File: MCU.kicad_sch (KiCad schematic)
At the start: 19 parts, among them J1 Conn_01x04, J5 Conn_01x03_Pin, J6 Conn_01x03_Pin, J7 Conn_01x03_Pin, J8 Conn_01x04, U2 STM32G431CBUx, X1 Crystal_Generic

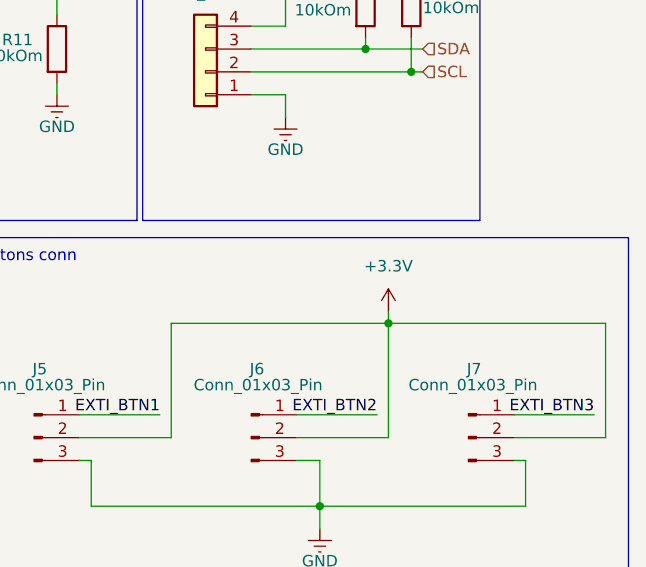
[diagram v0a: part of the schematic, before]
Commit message: Refactor PCB design parameters in endpoint-driver - Adjusted minimum hole-to-hole clearance from 0.25 to 0.24 in the .kicad_pro file for improved spacing.
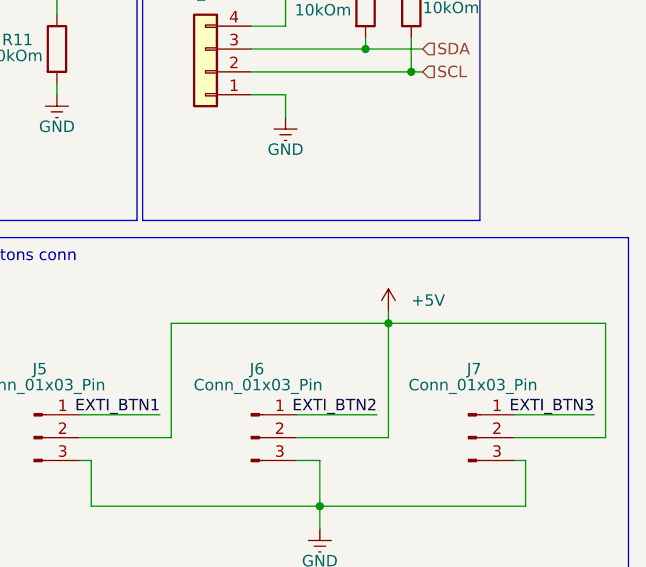
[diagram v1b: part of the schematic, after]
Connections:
- net +3.3V: no longer J5.2 (Pin_2), J6.2 (Pin_2), J7.2 (Pin_2)
- new net +5V: J5.2 (Pin_2), J6.2 (Pin_2), J7.2 (Pin_2)
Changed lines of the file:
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@@
 			)
 		)
-		(property "Value" "+3.3V"
-			(at 256.54 114.3 0)
+		(property "Value" "+5V"
+			(at 259.08 118.1099 0)
 			(effects
 				(font
 					(size 1.27 1.27)
 				)
+				(justify left)
 			)
 		)
